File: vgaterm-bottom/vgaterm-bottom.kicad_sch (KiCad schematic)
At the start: 72 parts, among them J10 Conn_01x14, J11 Conn_01x04, J12 Rst, J13 Conn_01x04, J14 Conn_01x02, J15 USB_B_Micro UART, J3 DE9_Receptacle, J4 RJ45_LED, J5 DE15_Receptacle_HighDensity_M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, J6 USB_B_Micro Debug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

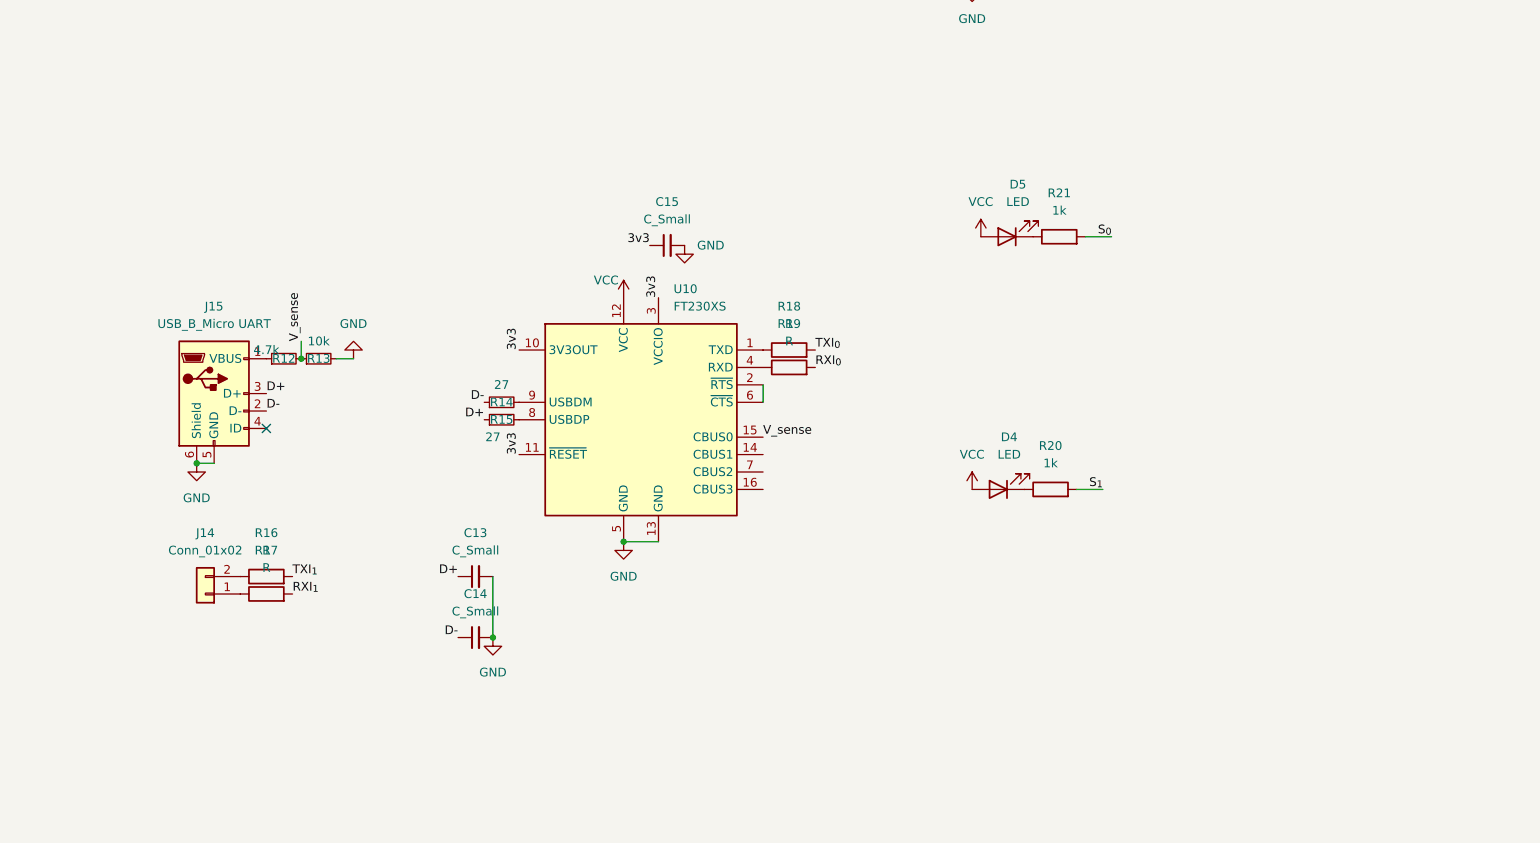
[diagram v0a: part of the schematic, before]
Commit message: initial rework for all smd on one side and all IO on bottom board
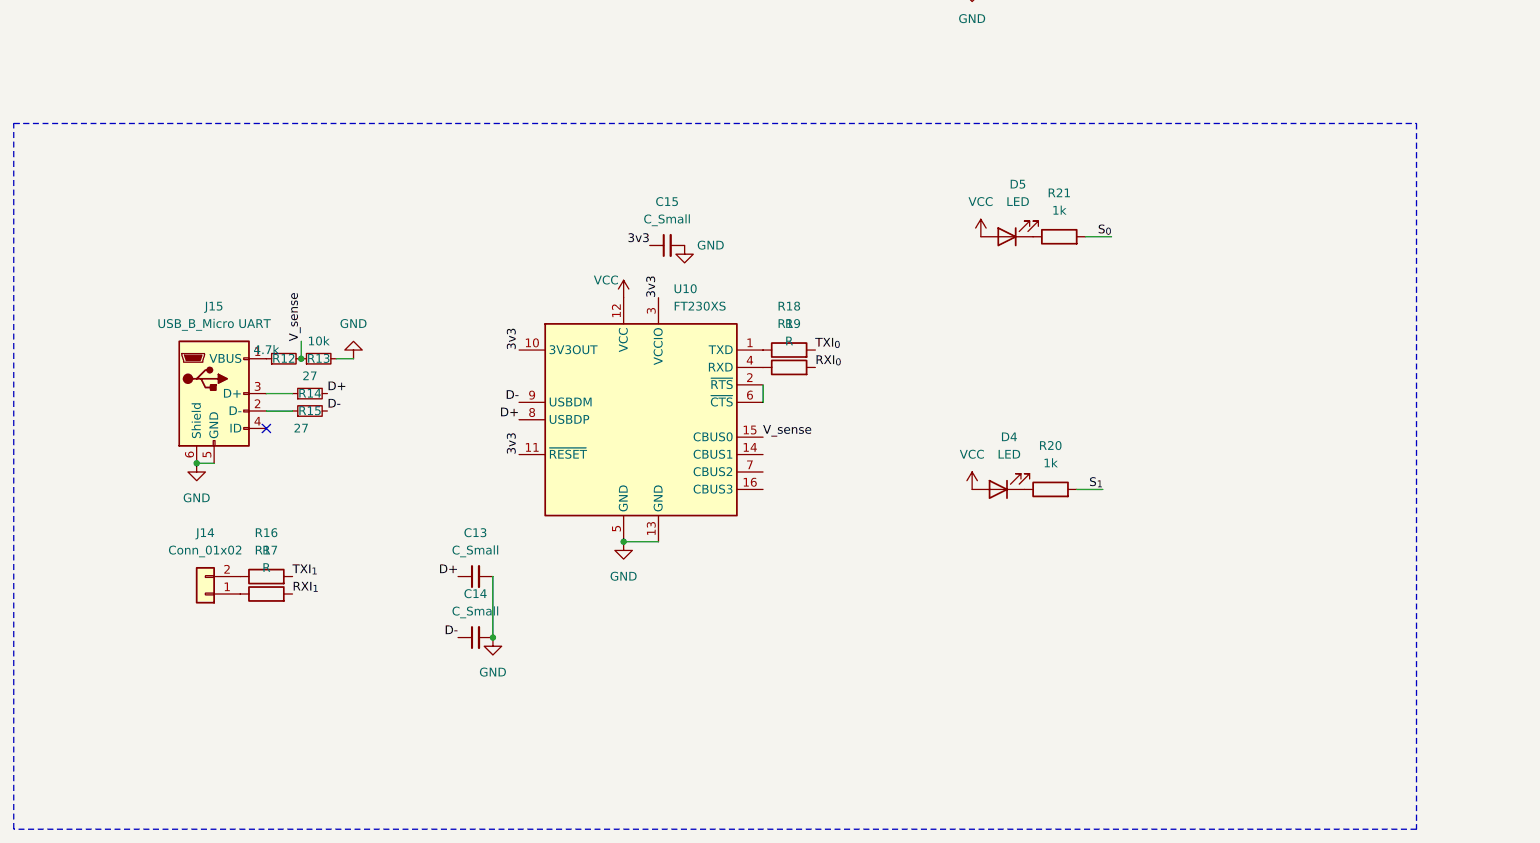
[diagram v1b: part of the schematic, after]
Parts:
- J10: footprint Connector_PinSocket_2.54mm:PinSocket_1x14_P2.54mm_Vertical_SMD_Pin1Left -> Connector_PinSocket_2.54mm:PinSocket_1x14_P2.54mm_Vertical
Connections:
- net D+: now also R14.2, U10.8 (USBDP); no longer J15.3 (D+), R15.1
- net D-: now also R15.2, U10.9 (USBDM); no longer J15.2 (D-), R14.1
- new net: J15.3 (D+), R14.1
- new net: J15.2 (D-), R15.1
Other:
- moved on the sheet: R14, R15
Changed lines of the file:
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@@
     (stroke (width 0) (type default))
   )
+  (wire (pts (xy 63.5 318.77) (xy 67.31 318.77))
+    (stroke (width 0) (type default))
+  )
   (wire (pts (xy 66.04 223.52) (xy 58.42 223.52))
     (stroke (width 0) (type default))
   )
+  (wire (pts (xy 63.5 321.31) (xy 67.31 321.31))
+    (stroke (width 0) (type default))
+  )
   (wire (pts (xy 87.63 153.67) (xy 87.63 158.75))
     (stroke (width 0) (type default))
@@
     (stroke (width 0) (type default))
   )
+  (rectangle (start 26.67 279.4) (end 231.14 382.27)
+    (stroke (width 0) (type dash))
+    (fill (type none))
+  )
   (text "CS" (at 232.41 181.61 0)
     (effects (font (size 1.27 1.27)) (justify left bottom))
@@
     (effects (font (size 1.27 1.27)) (justify left bottom))
   )
-  (label "D-" (at 63.5 321.31 0) (fields_autoplaced)
+  (label "D-" (at 72.39 321.31 0) (fields_autoplaced)
     (effects (font (size 1.27 1.27)) (justify left bottom))
   )
@@
     (effects (font (size 1.27 1.27)) (justify right bottom))
   )
-  (label "D+" (at 95.25 322.58 180) (fields_autoplaced)
+  (label "D+" (at 100.33 322.58 180) (fields_autoplaced)
     (effects (font (size 1.27 1.27)) (justify right bottom))
   )
@@
     (effects (font (size 1.27 1.27)) (justify right bottom))
   )
-  (label "D-" (at 95.25 320.04 180) (fields_autoplaced)
+  (label "D-" (at 100.33 320.04 180) (fields_autoplaced)
     (effects (font (size 1.27 1.27)) (justify right bottom))
   )
@@
     (effects (font (size 1.27 1.27)) (justify right bottom))
   )
-  (label "D+" (at 63.5 318.77 0) (fields_autoplaced)
+  (label "D+" (at 72.39 318.77 0) (fields_autoplaced)
     (effects (font (size 1.27 1.27)) (justify left bottom))
   )
@@
     )
   )
-  (symbol (lib_id "Device:R_Small") (at 97.79 320.04 90) (unit 1)
+  (symbol (lib_id "Device:R_Small") (at 69.85 318.77 90) (unit 1)
     (in_bom yes) (on_board yes) (dnp no)
-    (property "Reference" "R14" (at 97.79 320.04 90)
+    (property "Reference" "R14" (at 69.85 318.77 90)
       (effects (font (size 1.27 1.27)))
     )
-    (property "Value" "27" (at 97.79 317.5 90)
+    (property "Value" "27" (at 69.85 316.23 90)
       (effects (font (size 1.27 1.27)))
     )
-    (property "Footprint" "Resistor_SMD:R_0805_2012Metric_Pad1.20x1.40mm_HandSolder" (at 97.79 320.04 0)
+    (property "Footprint" "Resistor_SMD:R_0805_2012Metric_Pad1.20x1.40mm_HandSolder" (at 69.85 318.77 0)
       (effects (font (size 1.27 1.27)) hide)
     )
-    (property "Datasheet" "~" (at 97.79 320.04 0)
+    (property "Datasheet" "~" (at 69.85 318.77 0)
       (effects (font (size 1.27 1.27)) hide)
     )
@@
       (effects (font (size 1.27 1.27)))
     )
-    (property "Footprint" "Connector_PinSocket_2.54mm:PinSocket_1x14_P2.54mm_Vertical_SMD_Pin1Left" (at 367.03 138.43 0)
+    (property "Footprint" "Connector_PinSocket_2.54mm:PinSocket_1x14_P2.54mm_Vertical" (at 367.03 138.43 0)
       (effects (font (size 1.27 1.27)) hide)
     )
@@
     )
   )
-  (symbol (lib_id "Device:R_Small") (at 97.79 322.58 90) (unit 1)
+  (symbol (lib_id "Device:R_Small") (at 69.85 321.31 90) (unit 1)
     (in_bom yes) (on_board yes) (dnp no)
-    (property "Reference" "R15" (at 97.79 322.58 90)
+    (property "Reference" "R15" (at 69.85 321.31 90)
       (effects (font (size 1.27 1.27)))
     )
-    (property "Value" "27" (at 96.52 325.12 90)
+    (property "Value" "27" (at 68.58 323.85 90)
       (effects (font (size 1.27 1.27)))
     )
-    (property "Footprint" "Resistor_SMD:R_0805_2012Metric_Pad1.20x1.40mm_HandSolder" (at 97.79 322.58 0)
+    (property "Footprint" "Resistor_SMD:R_0805_2012Metric_Pad1.20x1.40mm_HandSolder" (at 69.85 321.31 0)
       (effects (font (size 1.27 1.27)) hide)
     )
-    (property "Datasheet" "~" (at 97.79 322.58 0)
+    (property "Datasheet" "~" (at 69.85 321.31 0)
       (effects (font (size 1.27 1.27)) hide)
     )
